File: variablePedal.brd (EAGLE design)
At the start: 42.9 x 67.3 mm, 16 parts, among them IC1 OPA340U, J2 AUDIO_JACK_TRS_0.25"_PTH_RA, J3 AUDIO_JACK_TRS_0.25"_PTH_RA, J4 5.5x2.1mm Barrel, Q1 MPSA56

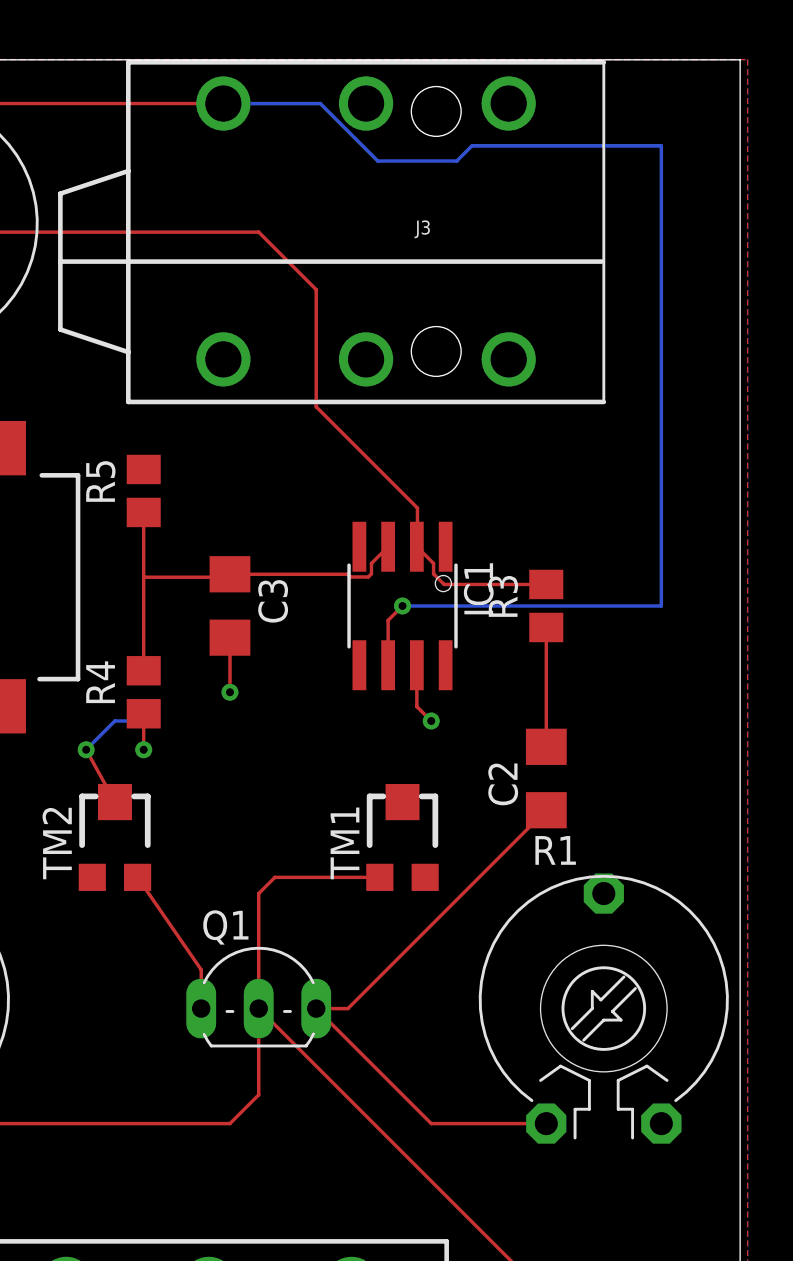
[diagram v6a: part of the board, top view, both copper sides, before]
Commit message: Updated schematic with socket, created BOM and Gerbers
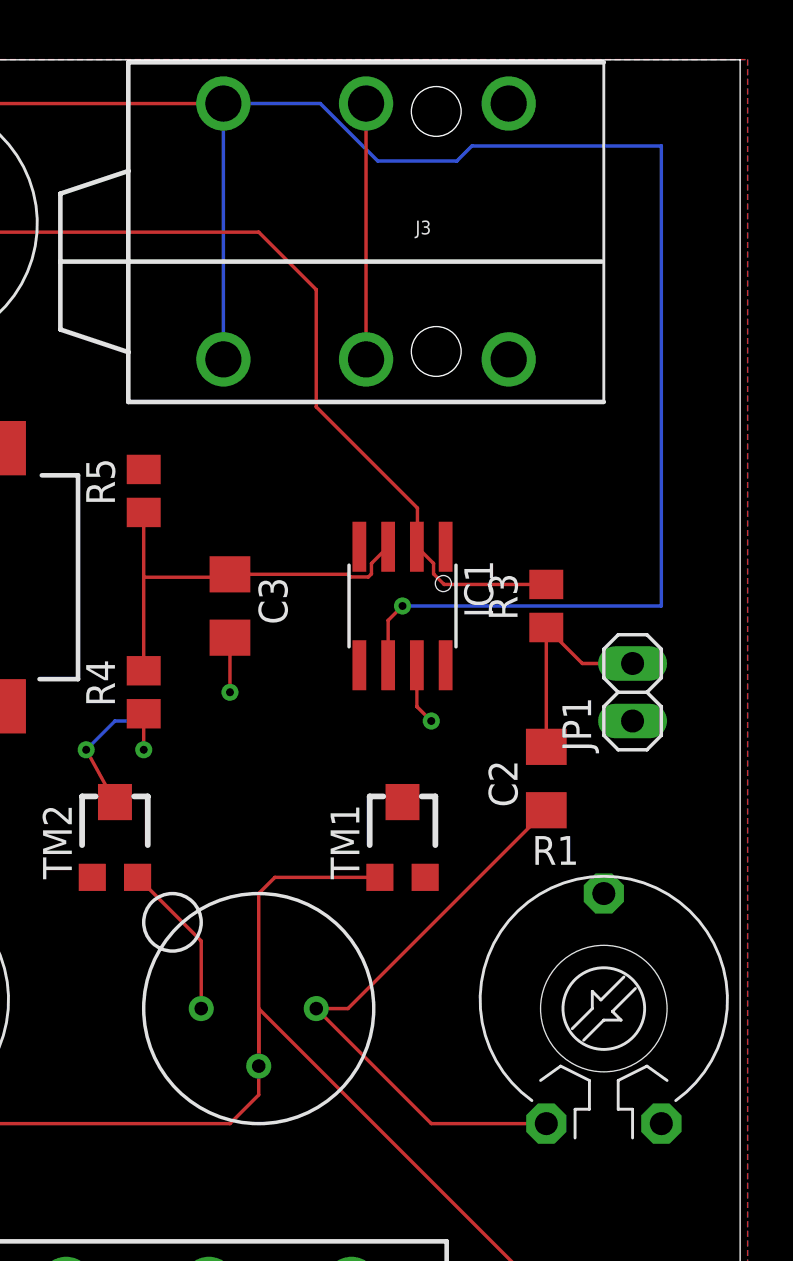
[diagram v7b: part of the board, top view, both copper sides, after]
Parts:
- removed Q1: MPSA56, transistor-pnp:TO92-CBE
- added JP1: (no value), pinhead:1X02
- added U$1: 917-43-103-41-005000, FormE:TO-5
- C1, C2, C3: value (none) -> CL31A106KOCLNNC
- R1: value (none) -> PT10MV10-504A2020-S
- R2: value (none) -> PT10MV11-103A2020-S
- R3, R4, R5: value (none) -> RMCF0805FT100K
- R6: value (none) -> PT10MV10-104A2020-S
- TM1: value (none) -> TC33X-1-104E
- TM2: value (none) -> TC33X-2-102E
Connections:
- new net N$8: J3.RING, J3.RING-NORM
- net GND: now also J3.SLEEVE-NORM, JP1.1
- net N$1: now also U$1.P$2; no longer Q1.B
- net N$2: now also U$1.P$3; no longer Q1.C
- net N$3: now also U$1.P$1; no longer Q1.E
- net N$4: now also JP1.2
- net N$7: now also J3.TIP-NORM
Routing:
- net N$8: track 0.00 -> 11.3 mm
- net N$7: track 69.2 -> 80.5 mm
- net N$4: track 5.27 -> 9.74 mm
- net N$1: track 52.3 -> 54.9 mm

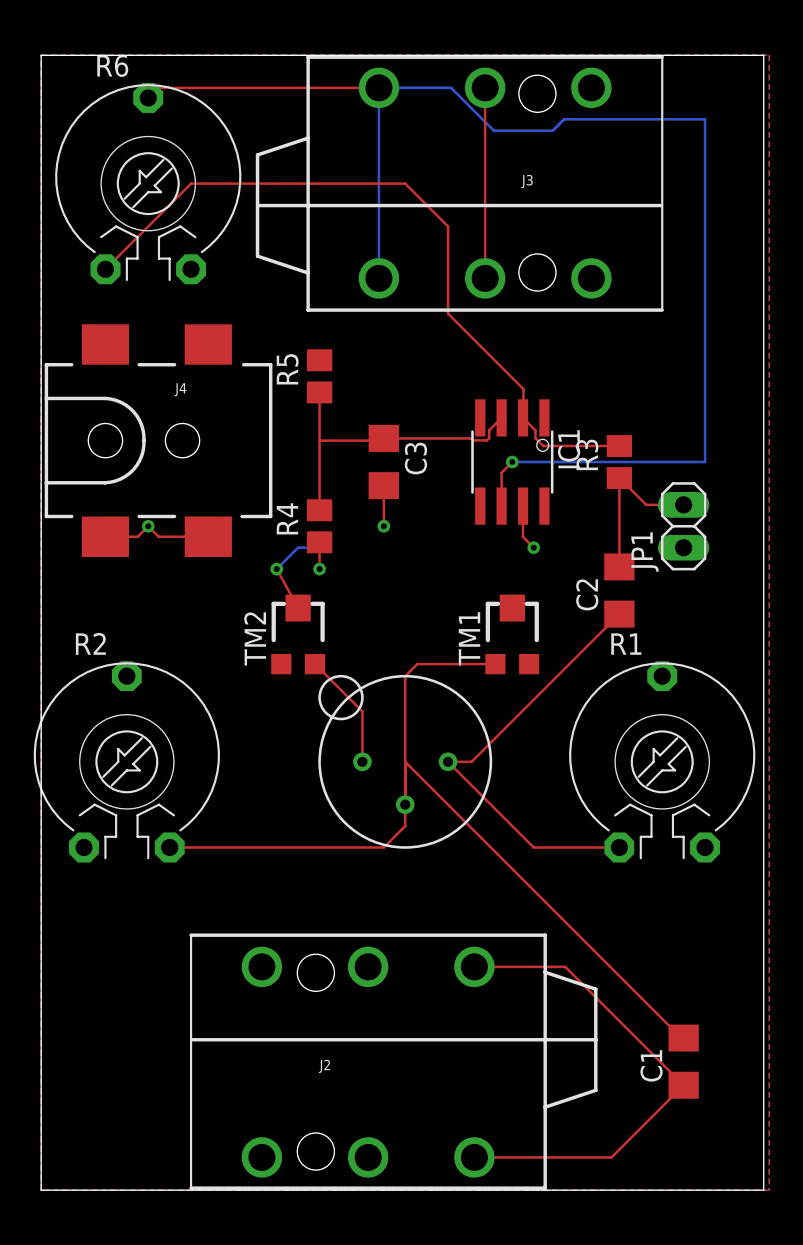
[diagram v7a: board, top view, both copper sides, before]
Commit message: added probe points, mounting holes and ordered!
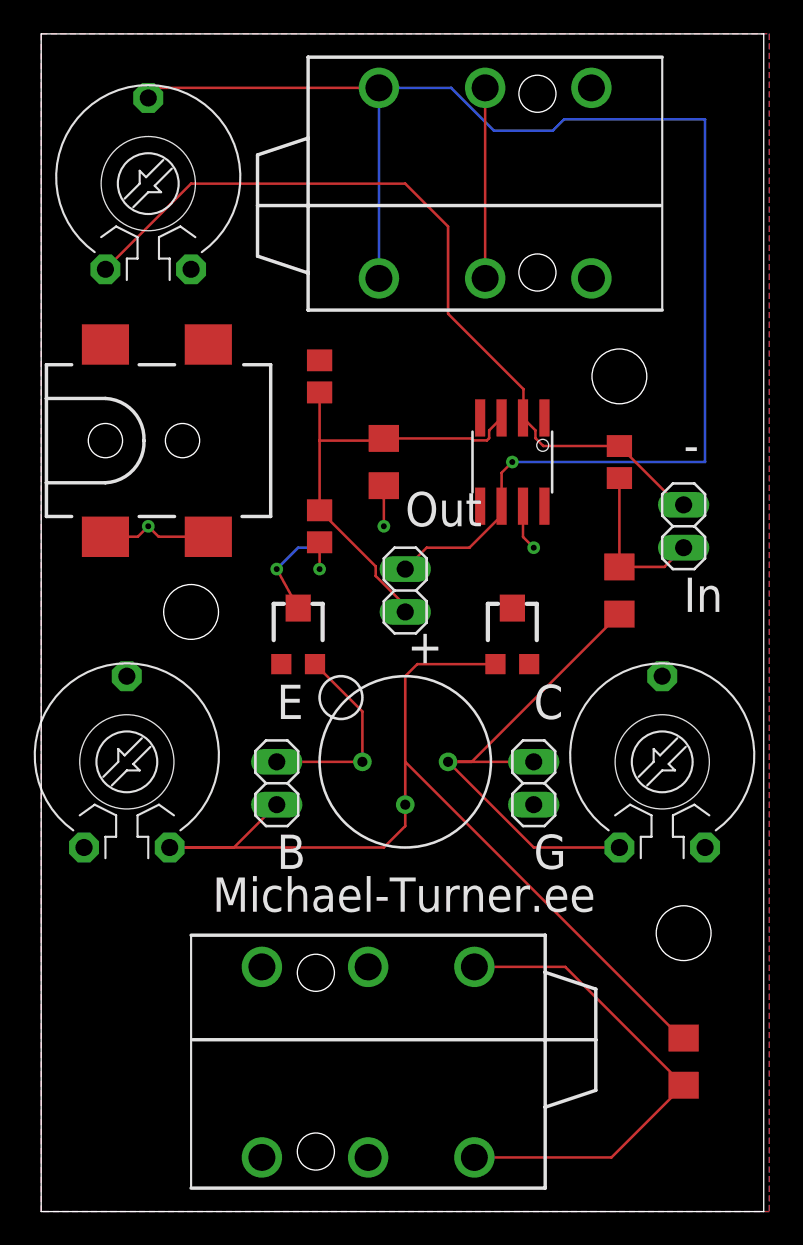
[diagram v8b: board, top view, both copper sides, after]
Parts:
- added JP2, JP3, JP4: (no value), pinhead:1X02
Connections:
- net GND: now also JP2.1; no longer JP1.1
- net N$1: now also JP3.1
- net N$2: now also JP2.2
- net N$3: now also JP3.2
- net N$4: now also JP1.1; no longer JP1.2
- net N$5: now also JP4.2
- net N$6: now also JP1.2
- net N$7: now also JP4.1
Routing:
- net N$5: track 18.7 -> 26.8 mm
- net N$7: track 80.5 -> 88.1 mm
- net N$6: track 43.4 -> 48.6 mm
- net N$2: track 26.1 -> 31.1 mm
- net N$3: track 6.96 -> 12.0 mm
- net N$1: track 54.9 -> 59.7 mm
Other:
- board size 42.9 x 67.3 mm -> 42.9 x 69.8 mm
- board text added: "+"
- board text added: "-"
- board text added: "B"
- board text added: "C"
- board text added: "E"
- board text added: "G"
- board text added: "In"
- board text added: "Michael-Turner.ee"
- board text added: "Out"
